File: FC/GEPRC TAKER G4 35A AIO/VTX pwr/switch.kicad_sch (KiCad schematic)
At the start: 2 parts, among them Q1 PMOS

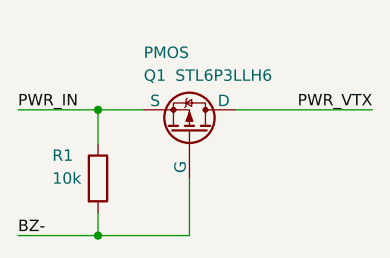
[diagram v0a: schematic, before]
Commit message: change VTX switch transistor
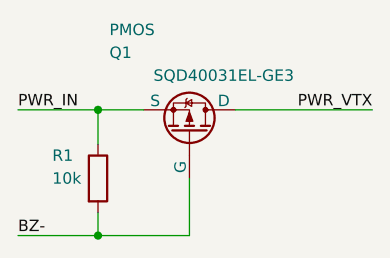
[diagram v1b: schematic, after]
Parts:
- Q1: Field8 STL6P3LLH6 -> SQD40031EL-GE3
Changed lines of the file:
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@@
 		(dnp no)
 		(property "Reference" "Q1"
-			(at 115.57 77.47 90)
+			(at 111.76 74.93 90)
 			(effects
 				(font
@@
 		)
 		(property "Value" "PMOS"
-			(at 115.57 74.93 90)
+			(at 111.76 72.39 90)
 			(effects
 				(font
@@
 			)
 		)
-		(property "Field8" "STL6P3LLH6"
+		(property "Field8" "SQD40031EL-GE3"
 			(at 124.46 77.47 90)
 			(effects
